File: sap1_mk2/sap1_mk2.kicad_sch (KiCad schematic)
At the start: 0 parts

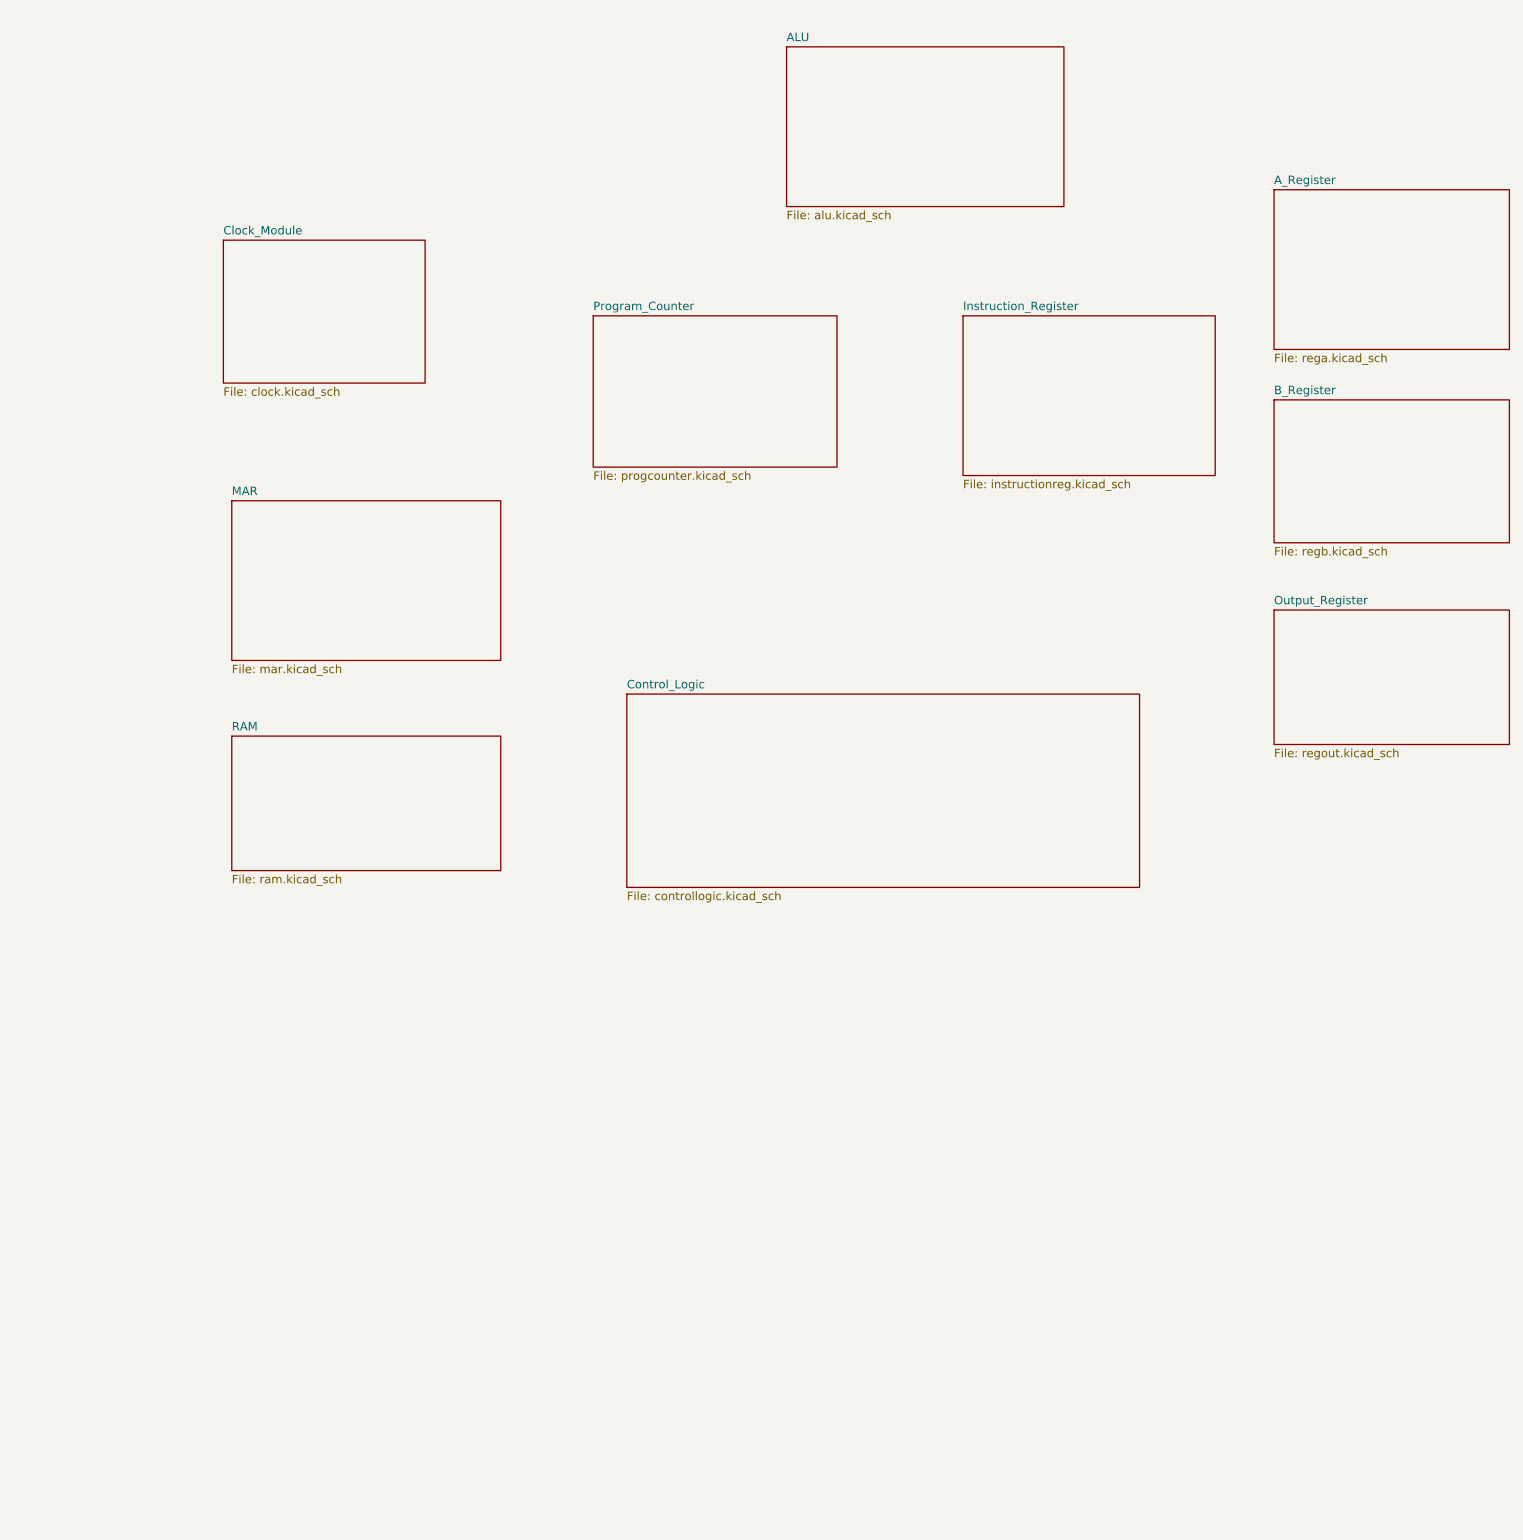
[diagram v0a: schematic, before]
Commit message: assigned footprints + finished root schematic
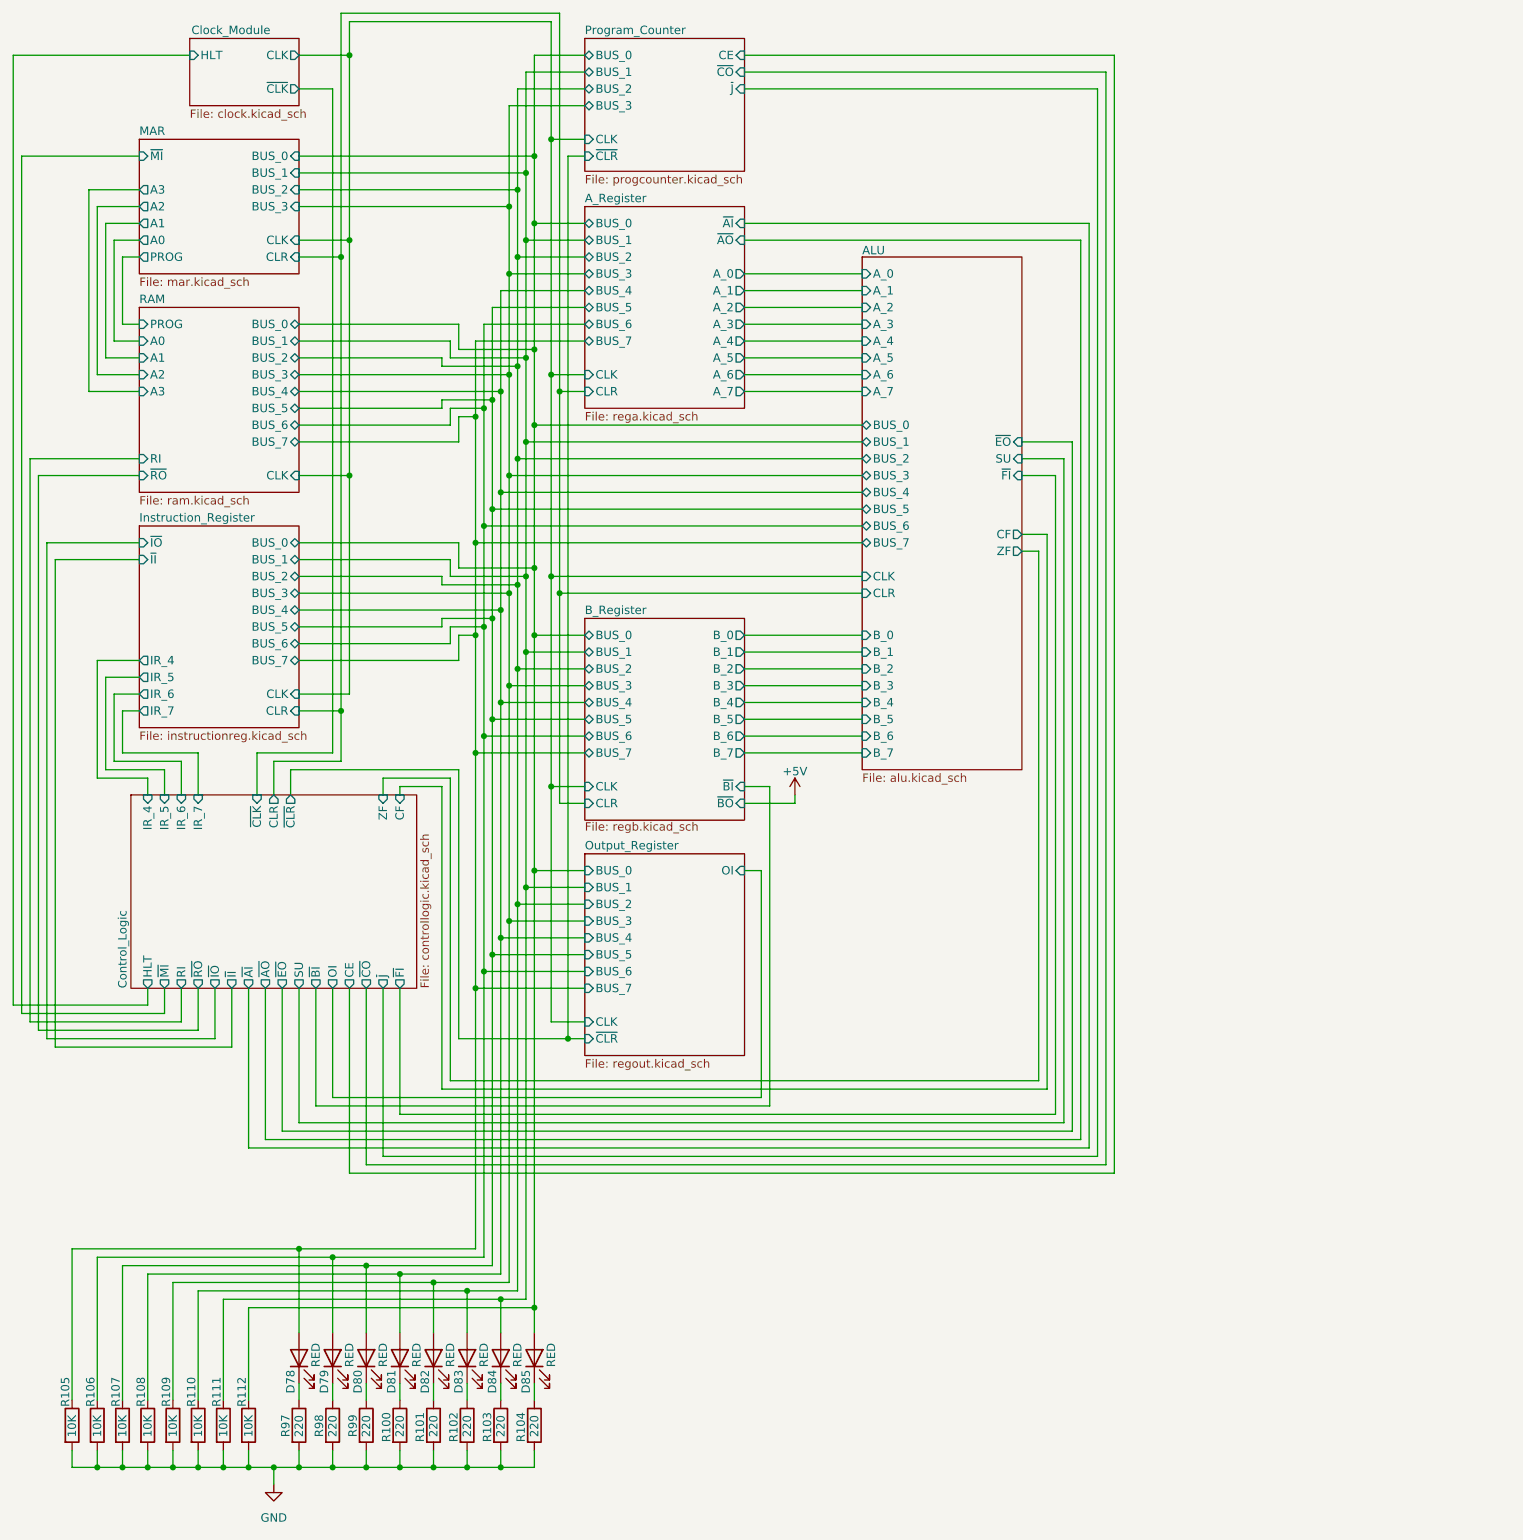
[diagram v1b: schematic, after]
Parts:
- added D78, D79, D80, D81, D82, D83, D84, D85: RED, LED_THT:LED_D3.0mm, symbol Device:LED
- added R100, R101, R102, R103, R104, R97, R98, R99: 220, Resistor_THT:R_Axial_DIN0207_L6.3mm_D2.5mm_P10.16mm_Horizontal, symbol Device:R
- added R105, R106, R107, R108, R109, R110, R111, R112: 10K, Resistor_THT:R_Axial_DIN0207_L6.3mm_D2.5mm_P10.16mm_Horizontal, symbol Device:R
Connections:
- new net: D81.1 (K), R100.1
- new net: D83.1 (K), R102.1
- new net: D80.1 (K), R99.1
- new net: D79.1 (K), R98.1
- new net: D82.1 (K), R101.1
- new net: D85.1 (K), R104.1
- new net: D78.1 (K), R97.1
- new net: D84.1 (K), R103.1
- new net ALU/BUS_0: D85.2 (A), R112.1
- new net ALU/BUS_1: D84.2 (A), R111.1
- new net ALU/BUS_2: D83.2 (A), R110.1
- new net ALU/BUS_3: D82.2 (A), R109.1
- new net ALU/BUS_4: D81.2 (A), R108.1
- new net ALU/BUS_5: D80.2 (A), R107.1
- new net ALU/BUS_6: D79.2 (A), R106.1
- new net ALU/BUS_7: D78.2 (A), R105.1
- new net GND: R100.2, R101.2, R102.2, R103.2, R104.2, R105.2, R106.2, R107.2, R108.2, R109.2, R110.2, R111.2, R112.2, R97.2, R98.2, R99.2
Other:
- sheet ALU ports: added A_0, A_1, A_2, A_3, A_4, A_5, A_6, A_7, BUS_0, BUS_1, BUS_2, BUS_3, BUS_4, BUS_5, BUS_6, BUS_7, B_0, B_1, B_2, B_3, B_4, B_5, B_6, B_7, CF, CLK, CLR, SU, ZF, ~{EO}, ~{FI}; removed none
- sheet A_Register ports: added A_0, A_1, A_2, A_3, A_4, A_5, A_6, A_7, BUS_0, BUS_1, BUS_2, BUS_3, BUS_4, BUS_5, BUS_6, BUS_7, CLK, CLR, ~{AI}, ~{AO}; removed none
- sheet B_Register ports: added BUS_0, BUS_1, BUS_2, BUS_3, BUS_4, BUS_5, BUS_6, BUS_7, B_0, B_1, B_2, B_3, B_4, B_5, B_6, B_7, CLK, CLR, ~{BI}, ~{BO}; removed none
- sheet Clock_Module ports: added CLK, HLT, ~{CLK}; removed none
- sheet Control_Logic ports: added CE, CF, CLR, HLT, IR_4, IR_5, IR_6, IR_7, OI, RI, SU, ZF, ~{AI}, ~{AO}, ~{BI}, ~{CLK}, ~{CLR}, ~{CO}, ~{EO}, ~{FI}, ~{II}, ~{IO}, ~{J}, ~{MI}, ~{RO}; removed none
- sheet Instruction_Register ports: added BUS_0, BUS_1, BUS_2, BUS_3, BUS_4, BUS_5, BUS_6, BUS_7, CLK, CLR, IR_4, IR_5, IR_6, IR_7, ~{II}, ~{IO}; removed none
- sheet MAR ports: added A0, A1, A2, A3, BUS_0, BUS_1, BUS_2, BUS_3, CLK, CLR, PROG, ~{MI}; removed none
- sheet Output_Register ports: added BUS_0, BUS_1, BUS_2, BUS_3, BUS_4, BUS_5, BUS_6, BUS_7, CLK, OI, ~{CLR}; removed none
- sheet Program_Counter ports: added BUS_0, BUS_1, BUS_2, BUS_3, CE, CLK, ~{CLR}, ~{CO}, ~{J}; removed none
- sheet RAM ports: added A0, A1, A2, A3, BUS_0, BUS_1, BUS_2, BUS_3, BUS_4, BUS_5, BUS_6, BUS_7, CLK, PROG, RI, ~{RO}; removed none

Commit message: export schematic files + update README.md
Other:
- title: (none) -> SAP-1 MK2
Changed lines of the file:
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@@
 	(paper "A4" portrait)
 	(title_block
+		(title "SAP-1 MK2")
+		(date "2026-04-19")
 		(rev "1.0")
 		(company "Purit (Kin) Hongjirakul")

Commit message: fixed unintended traces in B Register schematic
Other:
- title: SAP-1 MK2 -> SAP-1 Mk2
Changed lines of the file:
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@@
 	(paper "A4" portrait)
 	(title_block
-		(title "SAP-1 MK2")
+		(title "SAP-1 Mk2")
 		(date "2026-04-19")
 		(rev "1.0")

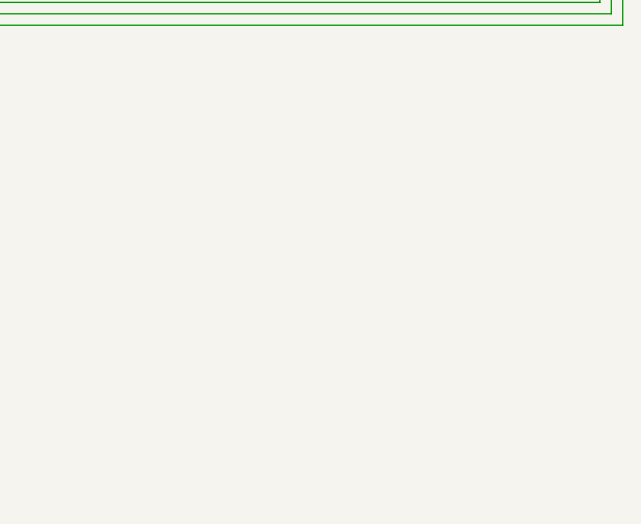
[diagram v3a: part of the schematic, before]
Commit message: placed PCB clock module
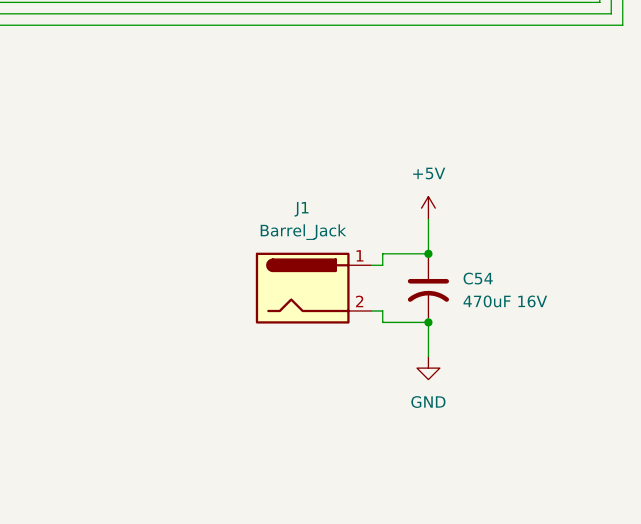
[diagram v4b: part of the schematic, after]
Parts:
- added C54: 470uF 16V, Capacitor_THT:CP_Radial_D4.0mm_P2.00mm, symbol Device:C_US
- added J1: Barrel_Jack, Connector_BarrelJack:BarrelJack_Horizontal, symbol Connector:Barrel_Jack
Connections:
- net +5V: now also C54.1, J1.1
- net GND: now also C54.2, J1.2
